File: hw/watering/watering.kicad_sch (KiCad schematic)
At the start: 0 parts

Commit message: progress
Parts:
- added AE1: Antenna_Shield, symbol Device:Antenna_Shield
- added J2: USB_C_Receptacle, symbol Connector:USB_C_Receptacle
- added U1: ESP32-C3, Package_DFN_QFN:QFN-32-1EP_5x5mm_P0.5mm_EP3.7x3.7mm, symbol MCU_Espressif:ESP32-C3
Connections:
- new net: J2.A1 (GND), J2.A12 (GND), J2.B1 (GND), J2.B12 (GND)
- new net: J2.A4 (VBUS), J2.A9 (VBUS), J2.B4 (VBUS), J2.B9 (VBUS)
- new net: U1.2 (VDD3P3), U1.3 (VDD3P3)
- new net: U1.31 (VDDA), U1.32 (VDDA)
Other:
- added sheet valves (valves.kicad_sch)

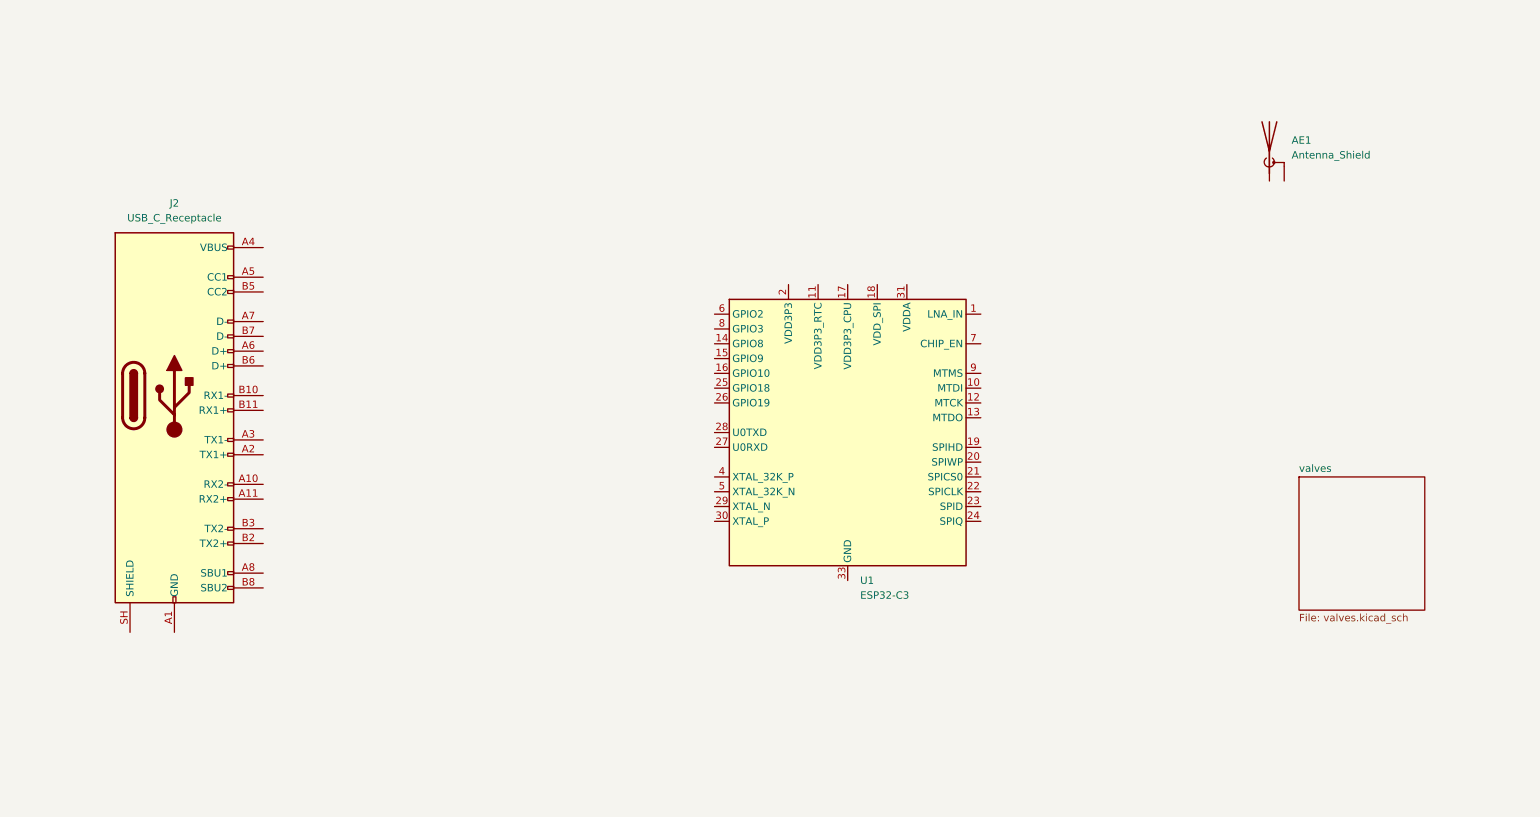
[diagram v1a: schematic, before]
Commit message: added esp32c6
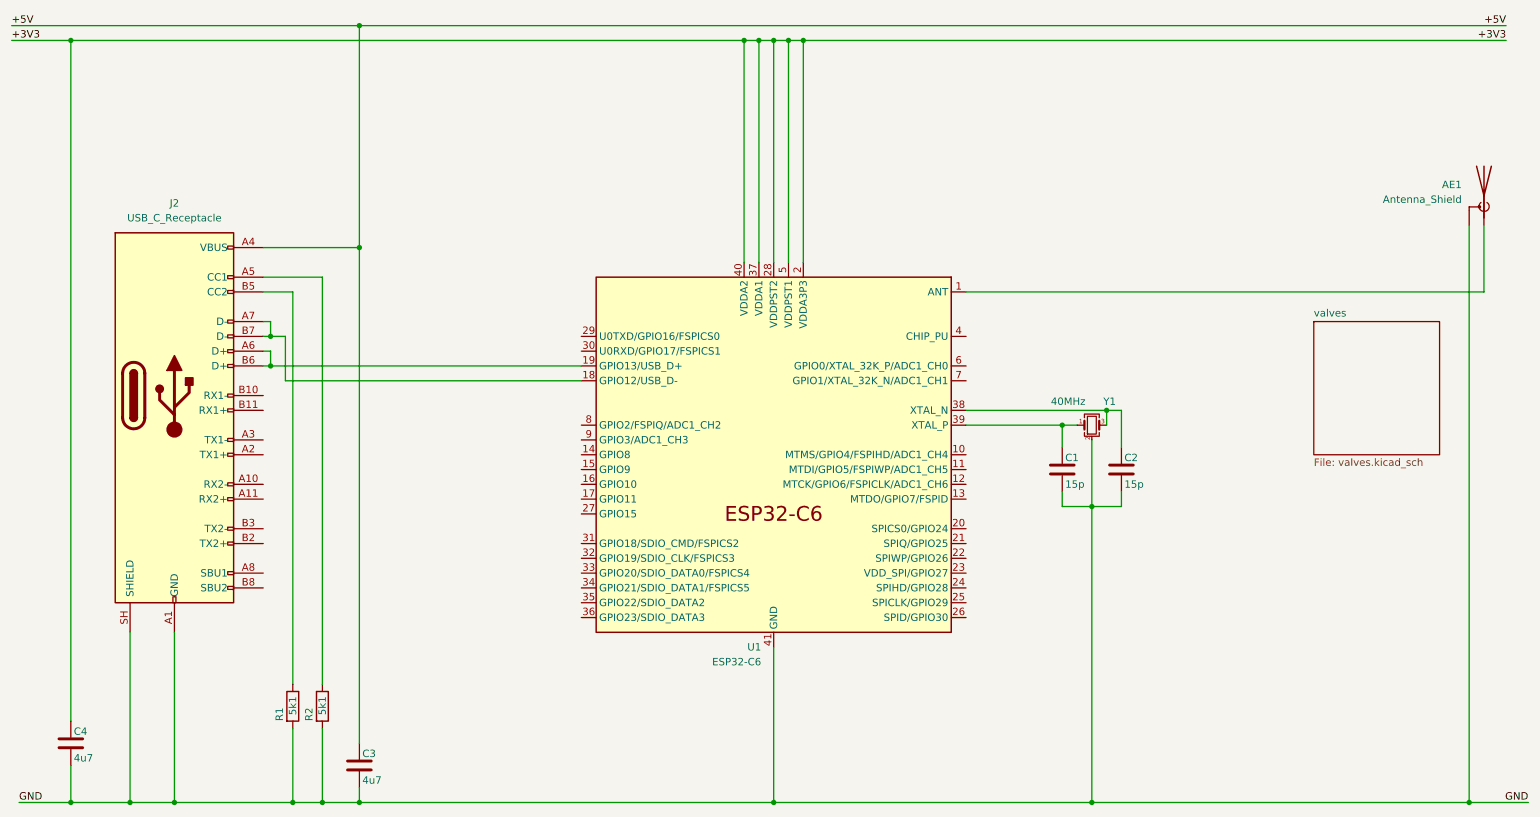
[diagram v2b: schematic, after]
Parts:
- removed U1: ESP32-C3, Package_DFN_QFN:QFN-32-1EP_5x5mm_P0.5mm_EP3.7x3.7mm, symbol MCU_Espressif:ESP32-C3
- added C1, C2: 15p, Capacitor_SMD:C_0603_1608Metric, symbol Device:C
- added C3, C4: 4u7, Capacitor_SMD:C_0603_1608Metric, symbol Device:C
- added R1, R2: 5k1, Resistor_SMD:R_0603_1608Metric, symbol Device:R
- added U1: ESP32-C6, Package_DFN_QFN:QFN-40-1EP_5x5mm_P0.4mm_EP3.6x3.6mm, symbol PCM_Espressif:ESP32-C6
- added Y1: 40MHz, symbol Device:Crystal_GND24_Small
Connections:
- net at AE1.1 (A): now also U1.1 (ANT)
- net GND: now reaches AE1.2 (Shield)
- net GND: now also J2.A1 (GND), J2.A12 (GND), J2.B1 (GND), J2.B12 (GND), J2.SH (SHIELD), C1.2, C2.2, C3.2, C4.2, R1.2, R2.2, U1.41 (GND), Y1.2 (G), Y1.4 (G)
- net +5V: now reaches J2.A4 (VBUS), J2.A9 (VBUS), J2.B4 (VBUS), J2.B9 (VBUS)
- net +5V: now also C3.1
- net at J2.A5 (CC1): now also R2.1
- net at J2.A6 (D+): now also J2.B6 (D+), U1.19 (GPIO13/USB_D+)
- net at J2.A7 (D-): now also J2.B7 (D-), U1.18 (GPIO12/USB_D-)
- net at J2.B5 (CC2): now also R1.1
- new net: C1.1, U1.39 (XTAL_P), Y1.1
- new net: C2.1, U1.38 (XTAL_N), Y1.3
- new net +3V3: C4.1, U1.2 (VDDA3P3), U1.28 (VDDPST2), U1.3 (VDDA3P3), U1.37 (VDDA1), U1.40 (VDDA2), U1.5 (VDDPST1)
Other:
- moved on the sheet: AE1

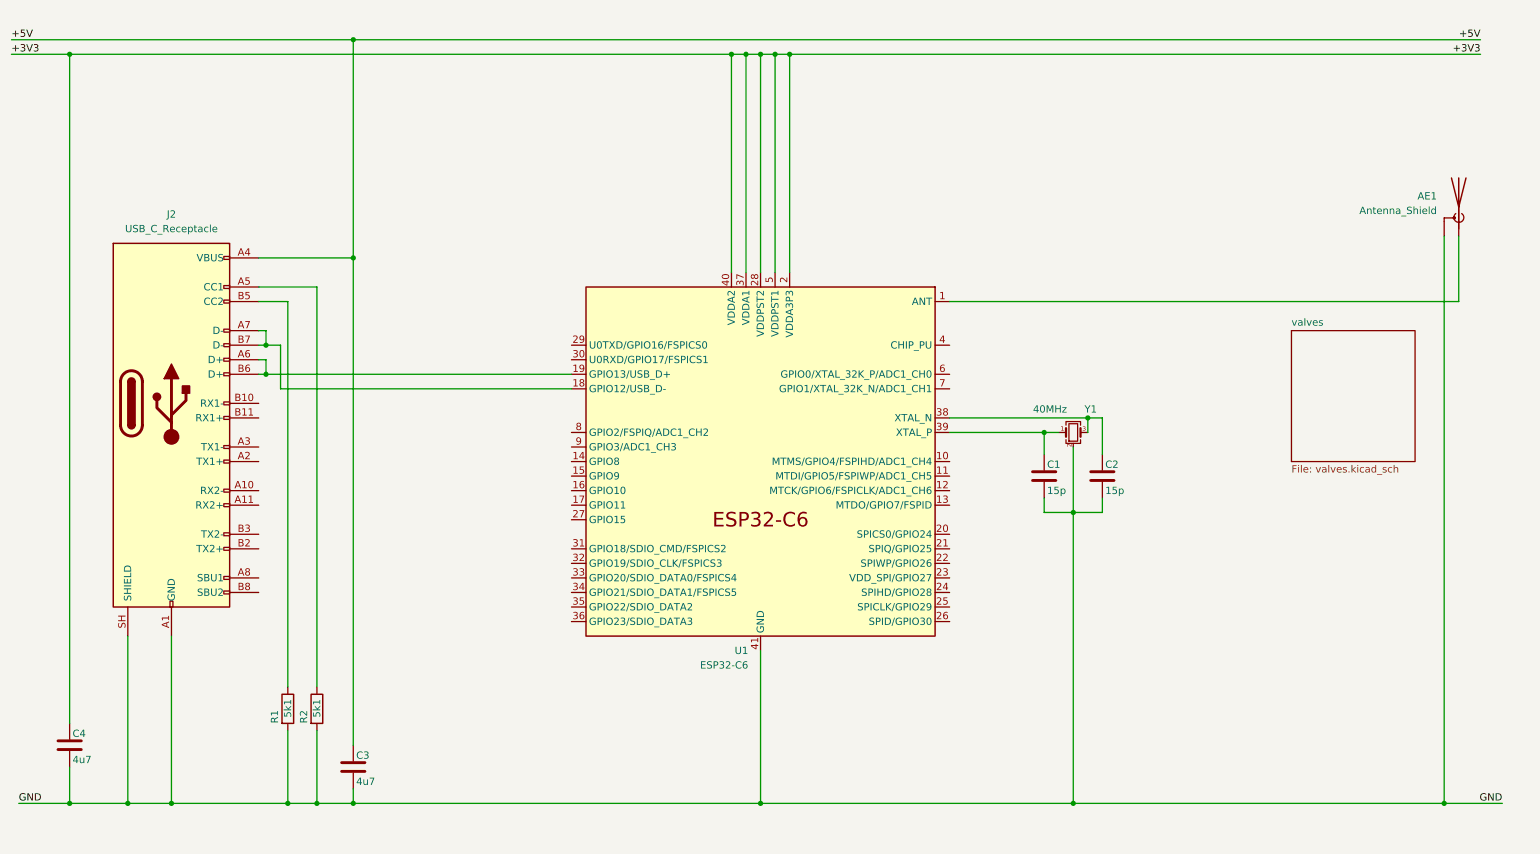
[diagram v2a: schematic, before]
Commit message: added battery management chip
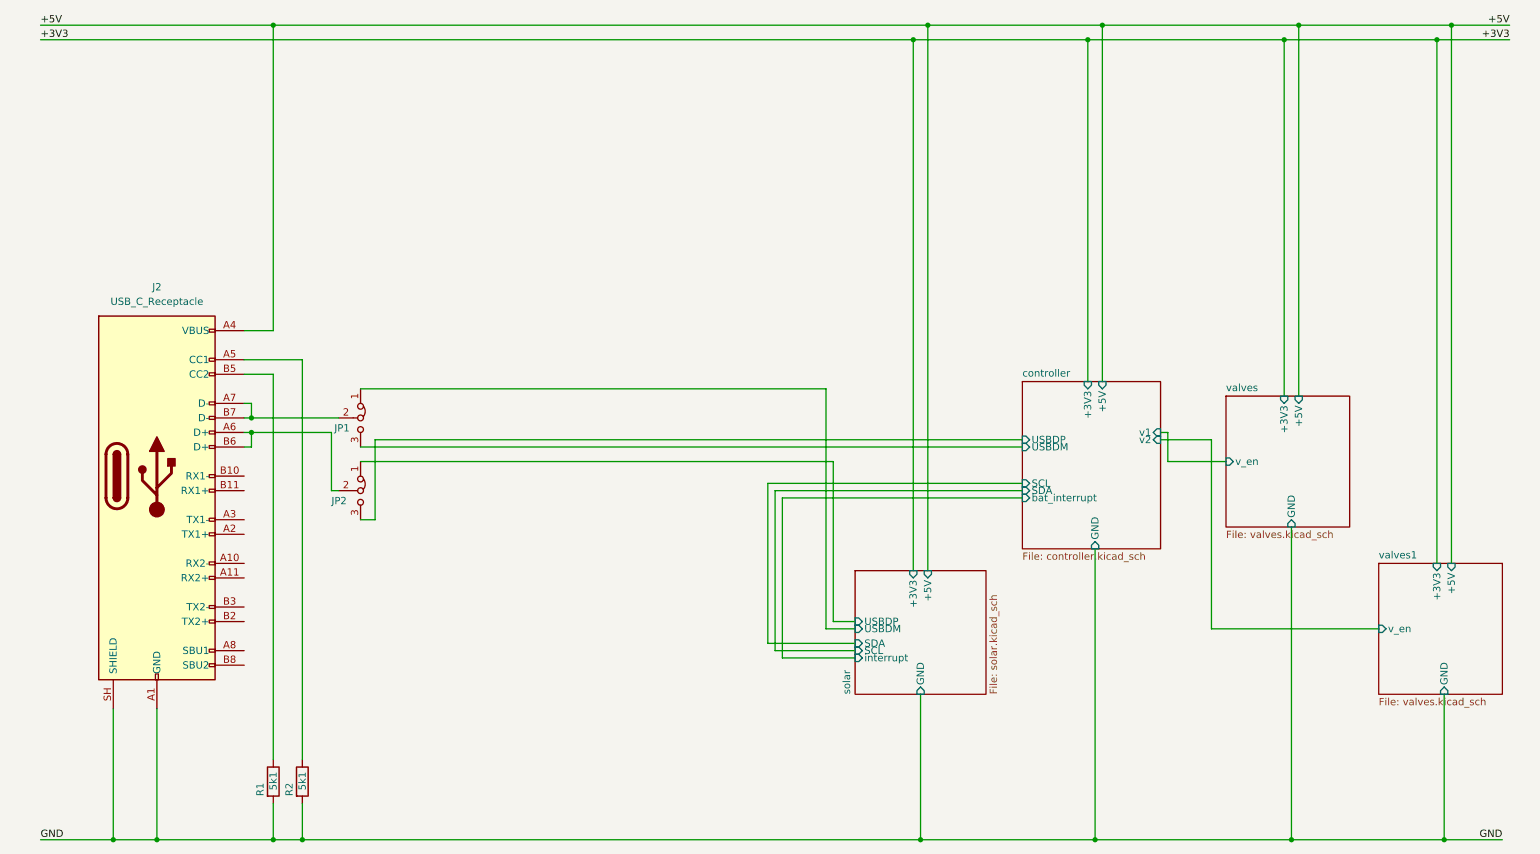
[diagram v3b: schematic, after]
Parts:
- removed AE1: Antenna_Shield, symbol Device:Antenna_Shield
- removed C1, C2: 15p, Capacitor_SMD:C_0603_1608Metric, symbol Device:C
- removed C3, C4: 4u7, Capacitor_SMD:C_0603_1608Metric, symbol Device:C
- removed U1: ESP32-C6, Package_DFN_QFN:QFN-40-1EP_5x5mm_P0.4mm_EP3.6x3.6mm, symbol PCM_Espressif:ESP32-C6
- removed Y1: 40MHz, symbol Device:Crystal_GND24_Small
- added JP1, JP2: Jumper_3_Bridged12, Connector_PinHeader_2.54mm:PinHeader_1x03_P2.54mm_Vertical, symbol Jumper:Jumper_3_Bridged12
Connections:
- net at J2.A6 (D+), J2.B6 (D+): now also JP2.2 (C)
- net at J2.A7 (D-), J2.B7 (D-): now also JP1.2 (C)
- new net controller/USBDM: JP1.3 (B)
- new net controller/USBDP: JP2.3 (B)
- new net solar/USBDM: JP1.1 (A)
- new net solar/USBDP: JP2.1 (A)
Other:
- added sheet controller (controller.kicad_sch)
- added sheet solar (solar.kicad_sch)
- added sheet valves1 (valves.kicad_sch)
- sheet valves ports: added +3V3, +5V, GND, v_en; removed none
